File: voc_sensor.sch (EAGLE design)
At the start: 14 parts, among them IC1 MP901, IC2 DS2438, IC3 7805DT, X1 MSTBV3

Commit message: changing some values: 5 Ohm resistor to 5.1 Ohm (5 Ohm is not broadly available) selected different type of TVS diode with essentially the same ratings
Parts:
- D1, D8: value SMA6F7.5A -> SMAJ7.5A-LF
- IC3: MANF# (none) -> MC7805BDTG
- R1, R2, R4: value 5 -> 5.1
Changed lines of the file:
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@@
 <grid distance="0.1" unitdist="inch" unit="inch" style="lines" multiple="1" display="no" altdistance="0.01" altunitdist="inch" altunit="inch"/>
 <layers>
-<layer number="1" name="Top" color="4" fill="1" visible="yes" active="no"/>
-<layer number="16" name="Bottom" color="1" fill="1" visible="yes" active="no"/>
-<layer number="17" name="Pads" color="2" fill="1" visible="yes" active="no"/>
-<layer number="18" name="Vias" color="2" fill="1" visible="yes" active="no"/>
-<layer number="19" name="Unrouted" color="6" fill="1" visible="yes" active="no"/>
-<layer number="20" name="Dimension" color="15" fill="1" visible="yes" active="no"/>
-<layer number="21" name="tPlace" color="7" fill="1" visible="yes" active="no"/>
-<layer number="22" name="bPlace" color="7" fill="1" visible="yes" active="no"/>
-<layer number="23" name="tOrigins" color="15" fill="1" visible="yes" active="no"/>
-<layer number="24" name="bOrigins" color="15" fill="1" visible="yes" active="no"/>
-<layer number="25" name="tNames" color="7" fill="1" visible="yes" active="no"/>
-<layer number="26" name="bNames" color="7" fill="1" visible="yes" active="no"/>
-<layer number="27" name="tValues" color="7" fill="1" visible="yes" active="no"/>
-<layer number="28" name="bValues" color="7" fill="1" visible="yes" active="no"/>
+<layer number="1" name="Top" color="4" fill="1" visible="no" active="no"/>
+<layer number="16" name="Bottom" color="1" fill="1" visible="no" active="no"/>
+<layer number="17" name="Pads" color="2" fill="1" visible="no" active="no"/>
+<layer number="18" name="Vias" color="2" fill="1" visible="no" active="no"/>
+<layer number="19" name="Unrouted" color="6" fill="1" visible="no" active="no"/>
+<layer number="20" name="Dimension" color="15" fill="1" visible="no" active="no"/>
+<layer number="21" name="tPlace" color="7" fill="1" visible="no" active="no"/>
+<layer number="22" name="bPlace" color="7" fill="1" visible="no" active="no"/>
+<layer number="23" name="tOrigins" color="15" fill="1" visible="no" active="no"/>
+<layer number="24" name="bOrigins" color="15" fill="1" visible="no" active="no"/>
+<layer number="25" name="tNames" color="7" fill="1" visible="no" active="no"/>
+<layer number="26" name="bNames" color="7" fill="1" visible="no" active="no"/>
+<layer number="27" name="tValues" color="7" fill="1" visible="no" active="no"/>
+<layer number="28" name="bValues" color="7" fill="1" visible="no" active="no"/>
 <layer number="29" name="tStop" color="7" fill="3" visible="no" active="no"/>
 <layer number="30" name="bStop" color="7" fill="6" visible="no" active="no"/>
@@
 <layer number="35" name="tGlue" color="7" fill="4" visible="no" active="no"/>
 <layer number="36" name="bGlue" color="7" fill="5" visible="no" active="no"/>
-<layer number="37" name="tTest" color="7" fill="1" visible="yes" active="no"/>
-<layer number="38" name="bTest" color="7" fill="1" visible="yes" active="no"/>
+<layer number="37" name="tTest" color="7" fill="1" visible="no" active="no"/>
+<layer number="38" name="bTest" color="7" fill="1" visible="no" active="no"/>
 <layer number="39" name="tKeepout" color="4" fill="11" visible="no" active="no"/>
 <layer number="40" name="bKeepout" color="1" fill="11" visible="no" active="no"/>
@@
 <layer number="44" name="Drills" color="7" fill="1" visible="no" active="no"/>
 <layer number="45" name="Holes" color="7" fill="1" visible="no" active="no"/>
-<layer number="46" name="Milling" color="3" fill="1" visible="yes" active="no"/>
-<layer number="47" name="Measures" color="7" fill="1" visible="yes" active="no"/>
-<layer number="48" name="Document" color="7" fill="1" visible="yes" active="no"/>
-<layer number="49" name="Reference" color="7" fill="1" visible="yes" active="no"/>
-<layer number="51" name="tDocu" color="7" fill="1" visible="yes" active="no"/>
-<layer number="52" name="bDocu" color="7" fill="1" visible="yes" active="no"/>
+<layer number="46" name="Milling" color="3" fill="1" visible="no" active="no"/>
+<layer number="47" name="Measures" color="7" fill="1" visible="no" active="no"/>
+<layer number="48" name="Document" color="7" fill="1" visible="no" active="no"/>
+<layer number="49" name="Reference" color="7" fill="1" visible="no" active="no"/>
+<layer number="51" name="tDocu" color="7" fill="1" visible="no" active="no"/>
+<layer number="52" name="bDocu" color="7" fill="1" visible="no" active="no"/>
 <layer number="91" name="Nets" color="2" fill="1" visible="yes" active="yes"/>
 <layer number="92" name="Busses" color="1" fill="1" visible="yes" active="yes"/>
@@
 <part name="IC1" library="sensor" deviceset="MP901" device=""/>
 <part name="IC2" library="1wire" deviceset="DS2438" device=""/>
-<part name="R1" library="rcl" deviceset="R-EU_" device="R0402" value="5"/>
-<part name="R2" library="rcl" deviceset="R-EU_" device="R0402" value="5"/>
-<part name="D8" library="diodes" deviceset="ZENER" device="" value="SMA6F7.5A"/>
+<part name="R1" library="rcl" deviceset="R-EU_" device="R0402" value="5.1"/>
+<part name="R2" library="rcl" deviceset="R-EU_" device="R0402" value="5.1"/>
+<part name="D8" library="diodes" deviceset="ZENER" device="" value="SMAJ7.5A-LF"/>
 <part name="X1" library="con-phoenix-508" deviceset="MSTBV3" device=""/>
 <part name="GND1" library="supply1" deviceset="GND" device=""/>
 <part name="GND2" library="supply1" deviceset="GND" device=""/>
 <part name="R3" library="rcl" deviceset="R-EU_" device="R0402" value="17k"/>
-<part name="IC3" library="linear" deviceset="78*" device="DT" technology="05"/>
+<part name="IC3" library="linear" deviceset="78*" device="DT" technology="05">
+<attribute name="MANF#" value="MC7805BDTG"/>
+</part>
 <part name="C1" library="rcl" deviceset="C-EU" device="C0805K" value="100n"/>
 <part name="C2" library="rcl" deviceset="C-EU" device="C0805K" value="1µ"/>
@@
 <part name="C4" library="rcl" deviceset="C-EU" device="C0805K" value="1µ"/>
 <part name="GND3" library="supply1" deviceset="GND" device=""/>
-<part name="D1" library="diodes" deviceset="ZENER" device="" value="SMA6F7.5A"/>
-<part name="R4" library="rcl" deviceset="R-EU_" device="R0402" value="5"/>
+<part name="D1" library="diodes" deviceset="ZENER" device="" value="SMAJ7.5A-LF"/>
+<part name="R4" library="rcl" deviceset="R-EU_" device="R0402" value="5.1"/>
 </parts>
 <sheets>
@@
 <instance part="GND2" gate="1" x="83.82" y="116.84"/>
 <instance part="R3" gate="G$1" x="83.82" y="129.54" rot="R90"/>
-<instance part="IC3" gate="A1" x="0" y="175.26"/>
+<instance part="IC3" gate="A1" x="0" y="175.26">
+<attribute name="MANF#" x="0" y="175.26" size="1.778" layer="96" display="off"/>
+</instance>
 <instance part="C1" gate="G$1" x="-20.32" y="170.18"/>
 <instance part="C2" gate="G$1" x="27.94" y="170.18"/>

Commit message: changing load resistor to 100k as stated on the sensor packaging... already tried this and it works like a charm
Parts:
- R3: value 17k -> 100k
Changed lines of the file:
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@@
 <part name="GND1" library="supply1" deviceset="GND" device=""/>
 <part name="GND2" library="supply1" deviceset="GND" device=""/>
-<part name="R3" library="rcl" deviceset="R-EU_" device="R0402" value="17k"/>
+<part name="R3" library="rcl" deviceset="R-EU_" device="R0402" value="100k"/>
 <part name="IC3" library="linear" deviceset="78*" device="DT" technology="05">
 <attribute name="MANF#" value="MC7805BDTG"/>

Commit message: replaced connector X1 to get a lower profile inside of the wall insert (resolves issue #2)
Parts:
- X1: value MSTBV3 -> SPRING_CLAMP_3_AST215; device con-phoenix-508:MSTBV3 -> connectors:SPRING_CLAMP_3_AST215
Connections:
- net N$10: now also X1-2.KL; no longer X1-2.1
- net N$4: now also X1-1.KL; no longer X1-1.1
- net N$5: now also X1-3.KL; no longer X1-3.1
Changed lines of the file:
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@@
 <part name="R2" library="rcl" deviceset="R-EU_" device="R0402" value="5.1"/>
 <part name="D8" library="diodes" deviceset="ZENER" device="" value="SMAJ7.5A-LF"/>
-<part name="X1" library="con-phoenix-508" deviceset="MSTBV3" device=""/>
 <part name="GND1" library="supply1" deviceset="GND" device=""/>
 <part name="GND2" library="supply1" deviceset="GND" device=""/>
@@
 <part name="D1" library="diodes" deviceset="ZENER" device="" value="SMAJ7.5A-LF"/>
 <part name="R4" library="rcl" deviceset="R-EU_" device="R0402" value="5.1"/>
+<part name="X1" library="connectors" deviceset="SPRING_CLAMP_3" device="_AST215"/>
 </parts>
 <sheets>
@@
 <instance part="R2" gate="G$1" x="-48.26" y="124.46"/>
 <instance part="D8" gate="G$1" x="-60.96" y="129.54" rot="R90"/>
-<instance part="X1" gate="-1" x="-91.44" y="134.62"/>
-<instance part="X1" gate="-2" x="-91.44" y="129.54"/>
-<instance part="X1" gate="-3" x="-91.44" y="124.46"/>
 <instance part="GND1" gate="1" x="0" y="116.84"/>
 <instance part="GND2" gate="1" x="83.82" y="116.84"/>
@@
 <instance part="D1" gate="G$1" x="-76.2" y="129.54" rot="R90"/>
 <instance part="R4" gate="G$1" x="-45.72" y="175.26"/>
+<instance part="X1" gate="-1" x="-86.36" y="134.62" rot="R180"/>
+<instance part="X1" gate="-2" x="-86.36" y="129.54" rot="R180"/>
+<instance part="X1" gate="-3" x="-86.36" y="124.46" rot="R180"/>
 </instances>
 <busses>
@@
 <junction x="-60.96" y="134.62"/>
 <pinref part="D8" gate="G$1" pin="C"/>
-<pinref part="X1" gate="-2" pin="1"/>
 <wire x1="-86.36" y1="129.54" x2="-66.04" y2="129.54" width="0.1524" layer="91"/>
 <wire x1="-66.04" y1="129.54" x2="-66.04" y2="134.62" width="0.1524" layer="91"/>
+<pinref part="X1" gate="-2" pin="KL"/>
 </segment>
 </net>
@@
 <net name="N$4" class="0">
 <segment>
-<pinref part="X1" gate="-1" pin="1"/>
 <wire x1="-86.36" y1="134.62" x2="-76.2" y2="134.62" width="0.1524" layer="91"/>
 <wire x1="-76.2" y1="134.62" x2="-76.2" y2="175.26" width="0.1524" layer="91"/>
@@
 <wire x1="-76.2" y1="132.08" x2="-76.2" y2="134.62" width="0.1524" layer="91"/>
 <junction x="-76.2" y="134.62"/>
+<pinref part="X1" gate="-1" pin="KL"/>
 </segment>
 </net>
@@
 <junction x="-60.96" y="124.46"/>
 <pinref part="D8" gate="G$1" pin="A"/>
-<pinref part="X1" gate="-3" pin="1"/>
 <pinref part="D1" gate="G$1" pin="A"/>
 <wire x1="-76.2" y1="127" x2="-76.2" y2="124.46" width="0.1524" layer="91"/>
 <junction x="-76.2" y="124.46"/>
+<pinref part="X1" gate="-3" pin="KL"/>
 </segment>
 </net>

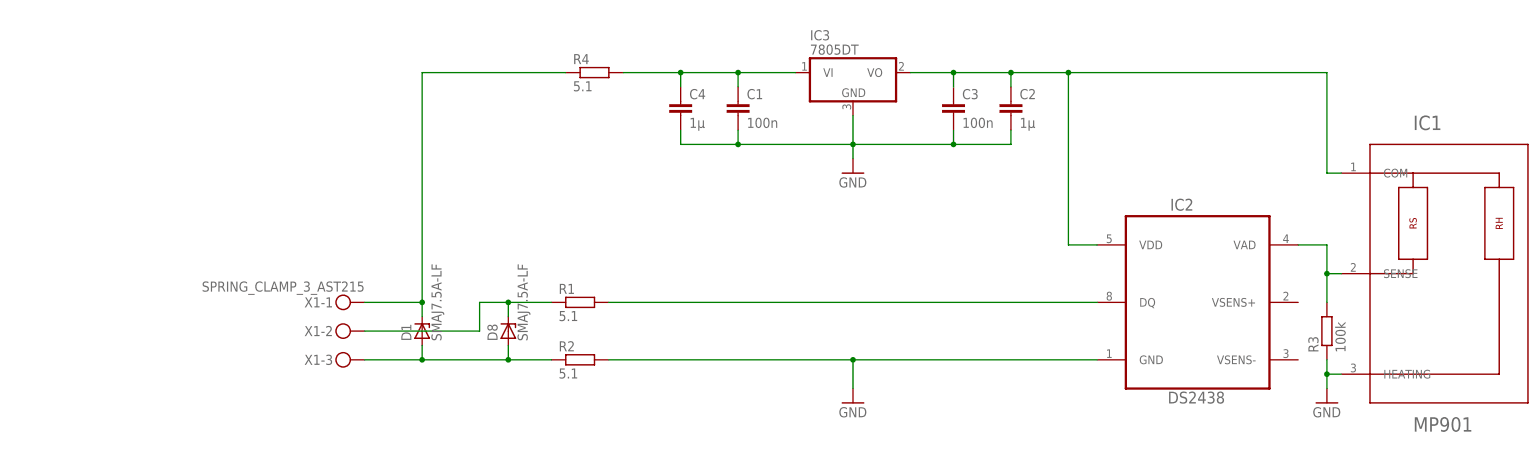
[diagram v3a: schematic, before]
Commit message: changing the 5V regulator to a switching type and adding some stuff to make the revision visible on the board without guesswork
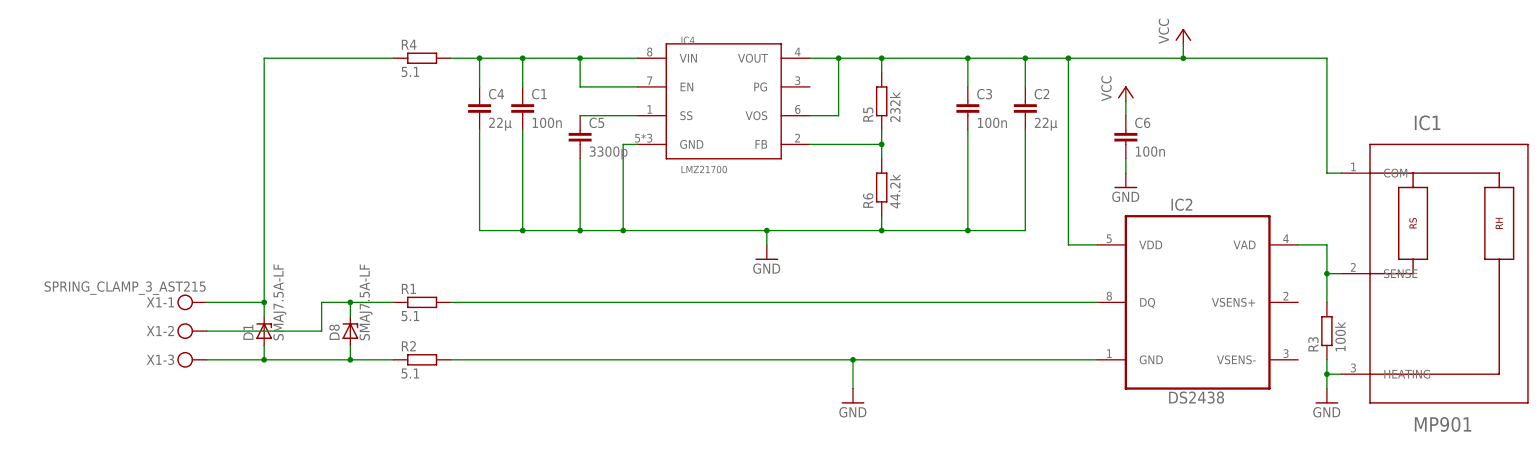
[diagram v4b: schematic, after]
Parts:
- removed IC3: 7805DT, linear:7805DT
- added C5: 3300p, rcl:C-EUC0402
- added C6: 100n, rcl:C-EUC0402
- added IC4: LMZ21700, ic_voltage_regulator:LMZ21700
- added R5: 232k, rcl:R-EU_R0402
- added R6: 44.2k, rcl:R-EU_R0402
- C1, C3: device rcl:C-EUC0805K -> rcl:C-EUC0402
- C2, C4: value 1µ -> 22µ
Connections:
- removed net N$2: C2.1, C3.1, IC1.COM, IC2.VDD, IC3.VO
- new net N$6: C5.1, IC4.SS
- new net N$7: IC4.FB, R5.1, R6.2
- new net VCC: C2.1, C3.1, C6.1, IC1.COM, IC2.VDD, IC4.VOS, IC4.VOUT, R5.2
- net GND: now also C5.2, C6.2, IC4.GND, R6.1; no longer IC3.GND
- net N$3: now also IC4.EN, IC4.VIN; no longer IC3.VI
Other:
- moved on the sheet: C1, C2, C3, C4, D1, D8, R1, R2, R4, X1-1, X1-2, X1-3

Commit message: adding voltage specifications to all capacitors solving issue #4
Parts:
- C1, C4, C5: VOLTAGE (none) -> >=25 V
- C2, C3, C6: VOLTAGE (none) -> >=6.3 V
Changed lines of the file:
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@@
 <grid distance="0.1" unitdist="inch" unit="inch" style="lines" multiple="1" display="no" altdistance="0.01" altunitdist="inch" altunit="inch"/>
 <layers>
-<layer number="1" name="Top" color="4" fill="1" visible="yes" active="no"/>
-<layer number="16" name="Bottom" color="1" fill="1" visible="yes" active="no"/>
-<layer number="17" name="Pads" color="2" fill="1" visible="yes" active="no"/>
-<layer number="18" name="Vias" color="2" fill="1" visible="yes" active="no"/>
-<layer number="19" name="Unrouted" color="6" fill="1" visible="yes" active="no"/>
-<layer number="20" name="Dimension" color="15" fill="1" visible="yes" active="no"/>
-<layer number="21" name="tPlace" color="7" fill="1" visible="yes" active="no"/>
-<layer number="22" name="bPlace" color="7" fill="1" visible="yes" active="no"/>
-<layer number="23" name="tOrigins" color="15" fill="1" visible="yes" active="no"/>
-<layer number="24" name="bOrigins" color="15" fill="1" visible="yes" active="no"/>
-<layer number="25" name="tNames" color="7" fill="1" visible="yes" active="no"/>
-<layer number="26" name="bNames" color="7" fill="1" visible="yes" active="no"/>
-<layer number="27" name="tValues" color="7" fill="1" visible="yes" active="no"/>
-<layer number="28" name="bValues" color="7" fill="1" visible="yes" active="no"/>
+<layer number="1" name="Top" color="4" fill="1" visible="no" active="no"/>
+<layer number="16" name="Bottom" color="1" fill="1" visible="no" active="no"/>
+<layer number="17" name="Pads" color="2" fill="1" visible="no" active="no"/>
+<layer number="18" name="Vias" color="2" fill="1" visible="no" active="no"/>
+<layer number="19" name="Unrouted" color="6" fill="1" visible="no" active="no"/>
+<layer number="20" name="Dimension" color="15" fill="1" visible="no" active="no"/>
+<layer number="21" name="tPlace" color="7" fill="1" visible="no" active="no"/>
+<layer number="22" name="bPlace" color="7" fill="1" visible="no" active="no"/>
+<layer number="23" name="tOrigins" color="15" fill="1" visible="no" active="no"/>
+<layer number="24" name="bOrigins" color="15" fill="1" visible="no" active="no"/>
+<layer number="25" name="tNames" color="7" fill="1" visible="no" active="no"/>
+<layer number="26" name="bNames" color="7" fill="1" visible="no" active="no"/>
+<layer number="27" name="tValues" color="7" fill="1" visible="no" active="no"/>
+<layer number="28" name="bValues" color="7" fill="1" visible="no" active="no"/>
 <layer number="29" name="tStop" color="7" fill="3" visible="no" active="no"/>
 <layer number="30" name="bStop" color="7" fill="6" visible="no" active="no"/>
@@
 <layer number="35" name="tGlue" color="7" fill="4" visible="no" active="no"/>
 <layer number="36" name="bGlue" color="7" fill="5" visible="no" active="no"/>
-<layer number="37" name="tTest" color="7" fill="1" visible="yes" active="no"/>
-<layer number="38" name="bTest" color="7" fill="1" visible="yes" active="no"/>
+<layer number="37" name="tTest" color="7" fill="1" visible="no" active="no"/>
+<layer number="38" name="bTest" color="7" fill="1" visible="no" active="no"/>
 <layer number="39" name="tKeepout" color="4" fill="11" visible="no" active="no"/>
 <layer number="40" name="bKeepout" color="1" fill="11" visible="no" active="no"/>
@@
 <layer number="44" name="Drills" color="7" fill="1" visible="no" active="no"/>
 <layer number="45" name="Holes" color="7" fill="1" visible="no" active="no"/>
-<layer number="46" name="Milling" color="3" fill="1" visible="yes" active="no"/>
-<layer number="47" name="Measures" color="7" fill="1" visible="yes" active="no"/>
-<layer number="48" name="Document" color="7" fill="1" visible="yes" active="no"/>
-<layer number="49" name="Reference" color="7" fill="1" visible="yes" active="no"/>
-<layer number="51" name="tDocu" color="7" fill="1" visible="yes" active="no"/>
-<layer number="52" name="bDocu" color="7" fill="1" visible="yes" active="no"/>
+<layer number="46" name="Milling" color="3" fill="1" visible="no" active="no"/>
+<layer number="47" name="Measures" color="7" fill="1" visible="no" active="no"/>
+<layer number="48" name="Document" color="7" fill="1" visible="no" active="no"/>
+<layer number="49" name="Reference" color="7" fill="1" visible="no" active="no"/>
+<layer number="51" name="tDocu" color="7" fill="1" visible="no" active="no"/>
+<layer number="52" name="bDocu" color="7" fill="1" visible="no" active="no"/>
 <layer number="91" name="Nets" color="2" fill="1" visible="yes" active="yes"/>
 <layer number="92" name="Busses" color="1" fill="1" visible="yes" active="yes"/>
@@
 <part name="GND2" library="supply1" deviceset="GND" device=""/>
 <part name="R3" library="rcl" deviceset="R-EU_" device="R0402" value="100k"/>
-<part name="C1" library="rcl" deviceset="C-EU" device="C0402" value="100n"/>
-<part name="C2" library="rcl" deviceset="C-EU" device="C0805K" value="22µ"/>
-<part name="C3" library="rcl" deviceset="C-EU" device="C0402" value="100n"/>
-<part name="C4" library="rcl" deviceset="C-EU" device="C0805K" value="22µ"/>
+<part name="C1" library="rcl" deviceset="C-EU" device="C0402" value="100n">
+<attribute name="VOLTAGE" value="&gt;=25 V"/>
+</part>
+<part name="C2" library="rcl" deviceset="C-EU" device="C0805K" value="22µ">
+<attribute name="VOLTAGE" value="&gt;=6.3 V"/>
+</part>
+<part name="C3" library="rcl" deviceset="C-EU" device="C0402" value="100n">
+<attribute name="VOLTAGE" value="&gt;=6.3 V"/>
+</part>
+<part name="C4" library="rcl" deviceset="C-EU" device="C0805K" value="22µ">
+<attribute name="VOLTAGE" value="&gt;=25 V"/>
+</part>
 <part name="GND3" library="supply1" deviceset="GND" device=""/>
 <part name="D1" library="diodes" deviceset="ZENER" device="" value="SMAJ7.5A-LF"/>
@@
 <part name="X1" library="connectors" deviceset="SPRING_CLAMP_3" device="_AST215"/>
 <part name="IC4" library="ic_voltage_regulator" deviceset="LMZ21700" device=""/>
-<part name="C5" library="rcl" deviceset="C-EU" device="C0402" value="3300p"/>
+<part name="C5" library="rcl" deviceset="C-EU" device="C0402" value="3300p">
+<attribute name="VOLTAGE" value="&gt;=25 V"/>
+</part>
 <part name="R5" library="rcl" deviceset="R-EU_" device="R0402" value="232k"/>
 <part name="R6" library="rcl" deviceset="R-EU_" device="R0402" value="44.2k"/>
-<part name="C6" library="rcl" deviceset="C-EU" device="C0402" value="100n"/>
+<part name="C6" library="rcl" deviceset="C-EU" device="C0402" value="100n">
+<attribute name="VOLTAGE" value="&gt;=6.3 V"/>
+</part>
 <part name="P+1" library="supply1" deviceset="VCC" device=""/>
 <part name="P+2" library="supply1" deviceset="VCC" device=""/>
@@
 <instance part="GND2" gate="1" x="83.82" y="116.84"/>
 <instance part="R3" gate="G$1" x="83.82" y="129.54" rot="R90"/>
-<instance part="C1" gate="G$1" x="-58.42" y="170.18"/>
-<instance part="C2" gate="G$1" x="30.48" y="170.18"/>
-<instance part="C3" gate="G$1" x="20.32" y="170.18"/>
-<instance part="C4" gate="G$1" x="-66.04" y="170.18"/>
+<instance part="C1" gate="G$1" x="-58.42" y="170.18">
+<attribute name="VOLTAGE" x="-58.42" y="170.18" size="1.778" layer="96" display="off"/>
+</instance>
+<instance part="C2" gate="G$1" x="30.48" y="170.18">
+<attribute name="VOLTAGE" x="30.48" y="170.18" size="1.778" layer="96" display="off"/>
+</instance>
+<instance part="C3" gate="G$1" x="20.32" y="170.18">
+<attribute name="VOLTAGE" x="20.32" y="170.18" size="1.778" layer="96" display="off"/>
+</instance>
+<instance part="C4" gate="G$1" x="-66.04" y="170.18">
+<attribute name="VOLTAGE" x="-66.04" y="170.18" size="1.778" layer="96" display="off"/>
+</instance>
 <instance part="GND3" gate="1" x="-15.24" y="142.24"/>
 <instance part="D1" gate="G$1" x="-104.14" y="129.54" rot="R90"/>
@@
 <instance part="X1" gate="-3" x="-114.3" y="124.46" rot="R180"/>
 <instance part="IC4" gate="G$1" x="-22.86" y="170.18"/>
-<instance part="C5" gate="G$1" x="-48.26" y="165.1"/>
+<instance part="C5" gate="G$1" x="-48.26" y="165.1">
+<attribute name="VOLTAGE" x="-48.26" y="165.1" size="1.778" layer="96" display="off"/>
+</instance>
 <instance part="R5" gate="G$1" x="5.08" y="170.18" rot="R90"/>
 <instance part="R6" gate="G$1" x="5.08" y="154.94" rot="R90"/>
-<instance part="C6" gate="G$1" x="48.26" y="165.1"/>
+<instance part="C6" gate="G$1" x="48.26" y="165.1">
+<attribute name="VOLTAGE" x="48.26" y="165.1" size="1.778" layer="96" display="off"/>
+</instance>
 <instance part="P+1" gate="VCC" x="58.42" y="182.88"/>
 <instance part="P+2" gate="VCC" x="48.26" y="172.72"/>
